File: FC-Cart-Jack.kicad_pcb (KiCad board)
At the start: 2 copper layers, 90 x 56.8 mm, 3 parts, among them J1 ToCartridge, J2 ToConsole

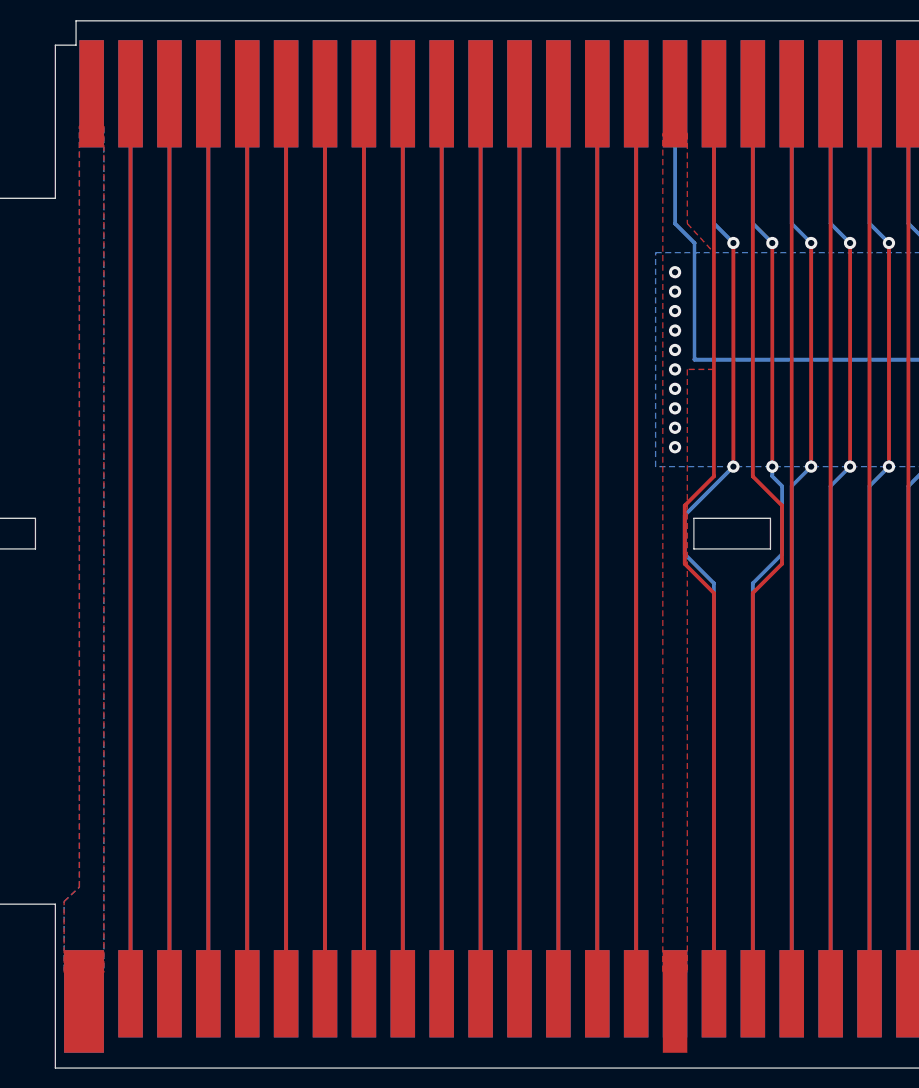
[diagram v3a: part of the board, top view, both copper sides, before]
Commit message: Optionally terminate audio with 100K resistor
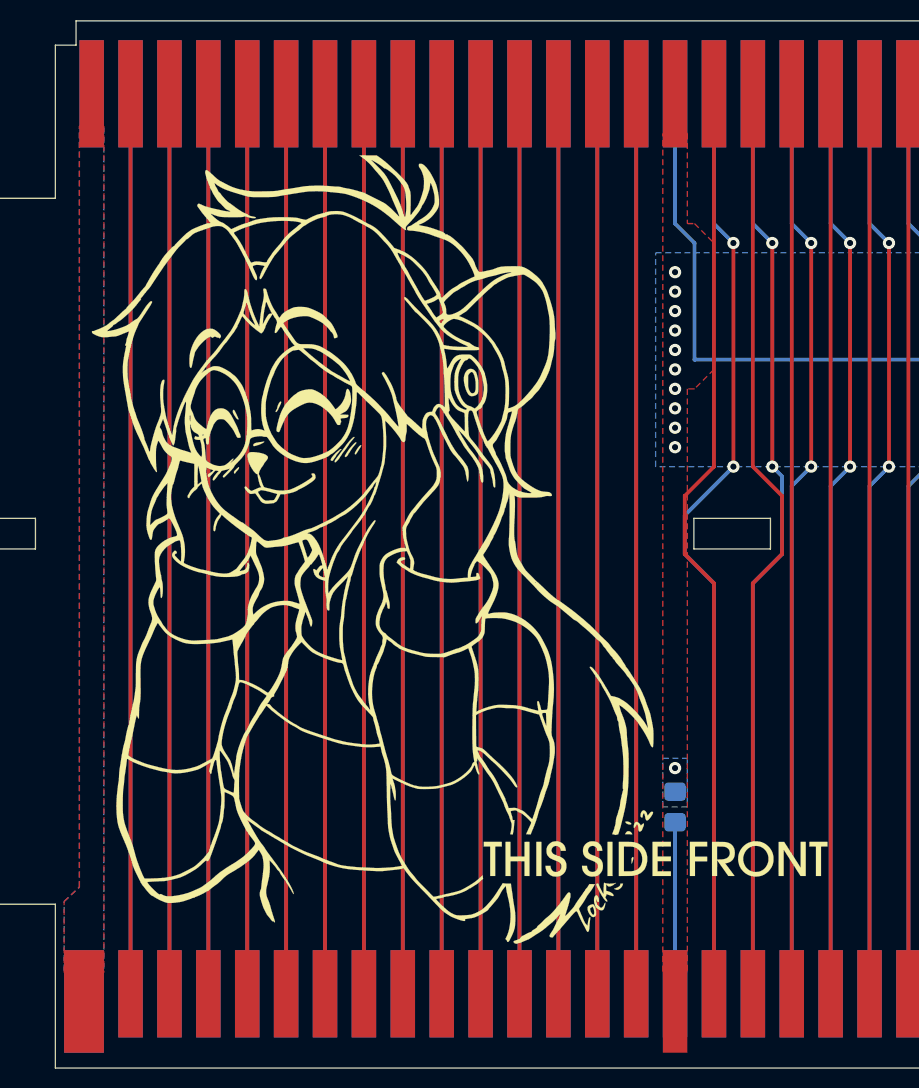
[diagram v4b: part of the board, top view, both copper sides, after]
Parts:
- added R1: 100K, Resistor_SMD:R_0805_2012Metric_Pad1.20x1.40mm_HandSolder, B.Cu at (128.3, 120.7)
- added Ref**: Val**, FC-Cart-Jack:FC-Cart-Jack-rounded-brd, F.Cu at (129.9, 103.5)
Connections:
- J2 pad 46: unconnected-(J2-Pad46) -> /AUD_RF
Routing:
- net /AUD_RF: track 0.00 -> 11.2 mm
- net GND: vias 10 -> 11

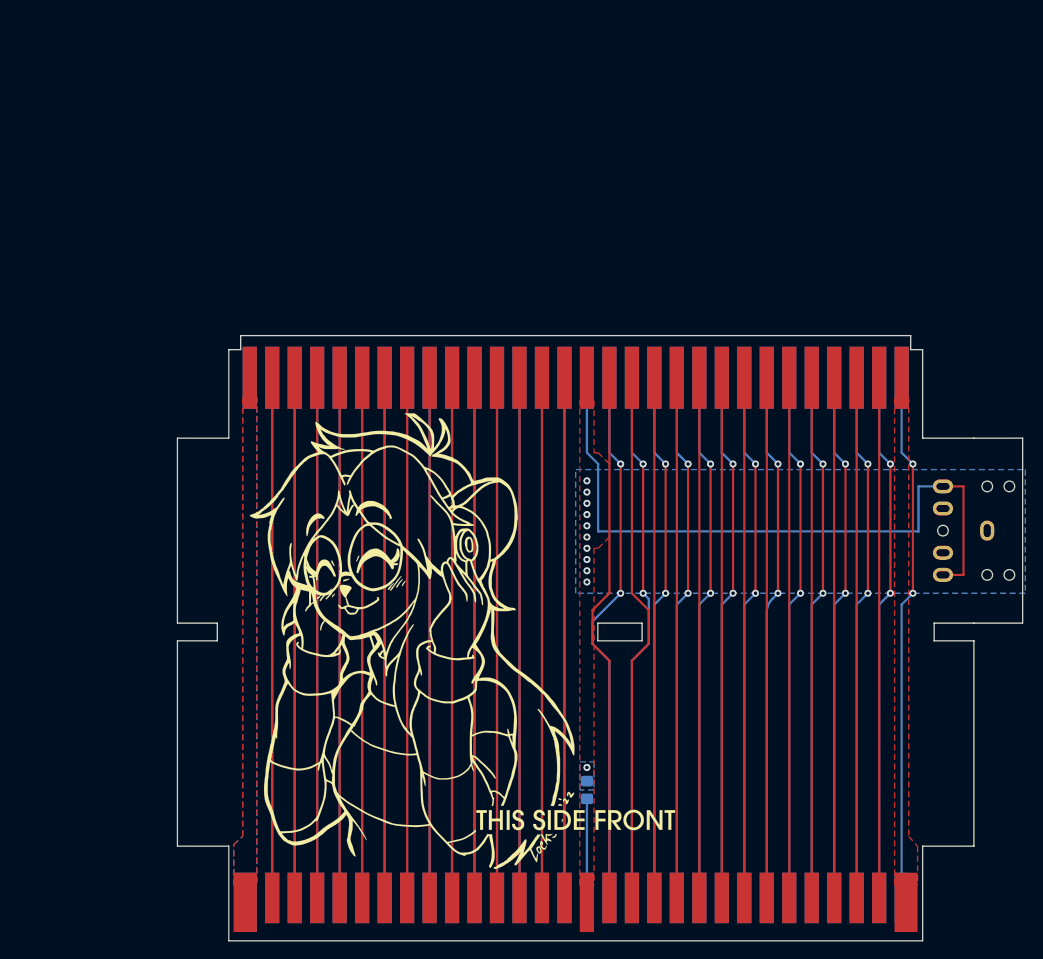
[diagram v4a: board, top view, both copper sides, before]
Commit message: Add new buffer circuit
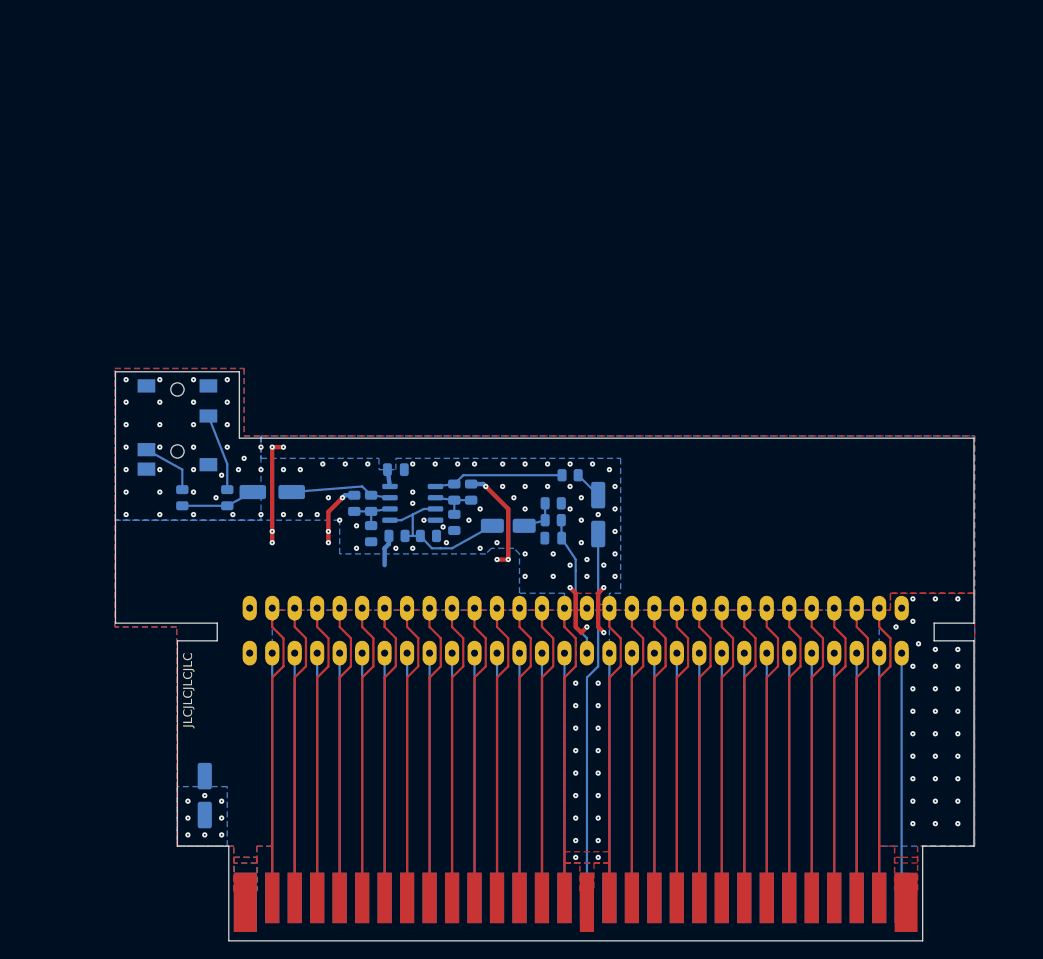
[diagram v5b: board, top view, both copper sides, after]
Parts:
- removed the J3 at (178.0, 91.3)
- removed Ref**: Val**, FC-Cart-Jack:FC-Cart-Jack-rounded-brd
- added C1: 0.1u, Capacitor_SMD:C_0805_2012Metric, B.Cu at (106.7, 84.5)
- added C2: 47u, Capacitor_SMD:CP_Elec_5x5.4, B.Cu at (85.1, 121.3)
- added C3: 47u, Capacitor_SMD:CP_Elec_5x5.4, B.Cu at (92.7, 87.0)
- added C4: 1u, Capacitor_SMD:CP_Elec_4x5.4, B.Cu at (119.4, 90.8)
- added C5: 1n, Capacitor_SMD:C_0805_2012Metric, B.Cu at (124.5, 92.2)
- added C6: 47u, Capacitor_SMD:CP_Elec_5x5.4, B.Cu at (129.5, 89.5)
- added J1: AudioOut, FC-Cart-Jack:Jack_3.5mm_PJ-342B-TX-SMT, B.Cu at (82.0, 72.8)
- added R10: 330, Resistor_SMD:R_0805_2012Metric, B.Cu at (126.4, 85.1)
- added R11: 47k, Resistor_SMD:R_0805_2012Metric, B.Cu at (115.2, 87.0)
- added R12: 82k, Resistor_SMD:R_0805_2012Metric, B.Cu at (113.3, 87.0)
- added R13: 68k, Resistor_SMD:R_0805_2012Metric, B.Cu at (113.3, 90.4)
- added R2: 330, Resistor_SMD:R_0805_2012Metric, B.Cu at (87.6, 87.6)
- added R3: 47k, Resistor_SMD:R_0805_2012Metric, B.Cu at (102.0, 88.3)
- added R4: 82k, Resistor_SMD:R_0805_2012Metric, B.Cu at (103.9, 88.3)
- added R5: 4.7k, Resistor_SMD:R_0805_2012Metric, B.Cu at (106.8, 91.9)
- added R6: 68k, Resistor_SMD:R_0805_2012Metric, B.Cu at (103.9, 91.7)
- added R7: 12k, Resistor_SMD:R_0805_2012Metric, B.Cu at (124.5, 90.2)
- added R8: 120k, Resistor_SMD:R_0805_2012Metric, B.Cu at (124.5, 88.3)
- added R9: 6.8k, Resistor_SMD:R_0805_2012Metric, B.Cu at (110.4, 91.9)
- added U1: TL972, Package_SO:SO-8_3.9x4.9mm_P1.27mm, B.Cu at (108.6, 88.3)
- J2: renamed from J1; footprint FC-Cart-Jack:card edge -> FC-Cart-Jack:FC_CONN_F; moved to B.Cu
- R1: value 100K -> 330; footprint Resistor_SMD:R_0805_2012Metric_Pad1.20x1.40mm_HandSolder -> Resistor_SMD:R_0805_2012Metric
- moved R1 56.4 mm to (82.5, 87.6)
- moved J2 21.8 mm to (127.0, 102.7)
- renumbered J2 to J3
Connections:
- R1 pad 1: /AUD_RF -> /AUD_JACK
- R1 pad 2: GND -> Net-(J1-PadT)
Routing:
- net /AUD_Output: track 76.6 -> 16.0 mm
- net VCC: track 0.00 -> 37.0 mm, vias 0 -> 42
- net /PPU_~{WR}: track 61.4 -> 27.7 mm, vias 2 -> 0
- net /CIRAM_~{CE}: track 60.4 -> 27.7 mm, vias 2 -> 0
- net /PPU_~{A13}: track 59.8 -> 27.7 mm, vias 2 -> 0
- net /PPU_D6: track 59.8 -> 27.7 mm, vias 2 -> 0
- net /PPU_D5: track 59.8 -> 27.7 mm, vias 2 -> 0
- net /PPU_A9: track 59.8 -> 27.7 mm, vias 2 -> 0
- net /PPU_A8: track 59.8 -> 27.7 mm, vias 2 -> 0
- net /PPU_A13: track 59.8 -> 27.7 mm, vias 2 -> 0
- net /PPU_A12: track 59.8 -> 27.7 mm, vias 2 -> 0
- net /PPU_D4: track 59.8 -> 27.7 mm, vias 2 -> 0
- net /PPU_D7: track 59.8 -> 27.7 mm, vias 2 -> 0
- net /PPU_A7: track 59.8 -> 27.7 mm, vias 2 -> 0
- net /PPU_A10: track 59.8 -> 27.7 mm, vias 2 -> 0
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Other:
- board size 90 x 56.8 mm -> 97 x 64.3 mm
